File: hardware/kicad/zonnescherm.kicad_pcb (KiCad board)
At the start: 2 copper layers, 75 x 75 mm, 28 parts, among them K1 K1-ON/OFF, K2 K1-UP/DOWN, K3 K2-ON/OFF, K4 K2-UP/DOWN, P1 ARDUINO-ISP, P2 CONN_MAINS, P3 CONN_SUNSHADE1, P4 CONN_SUNSHADE2, P5 SWITCHES, U1 IRM-05-5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

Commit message: Added high voltage logo
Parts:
- added C6: 100n, Capacitors_SMD:C_0805_HandSoldering, B.Cu at (120.7, 109.2)
- added C7: 100n, Capacitors_SMD:C_0805_HandSoldering, B.Cu at (138.7, 109.2)
- added G***: LOGO, modex:high_voltage_logo, B.Cu at (158.5, 95.0)
- added R8: 390, Resistors_SMD:R_0805_HandSoldering, B.Cu at (117.9, 109.2)
- P5: footprint Pin_Headers:Pin_Header_Straight_2x04 -> Pin_Headers:Pin_Header_Straight_2x05
- moved G*** 0.36 mm to (132.6, 129.0)
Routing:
- net P3V3: track 77.0 -> 103.8 mm
- net GND: track 168.7 -> 161.4 mm
- net Net-(P5-Pad10): track 0.00 -> 3.21 mm
- net P5V: track 88.9 -> 91.7 mm

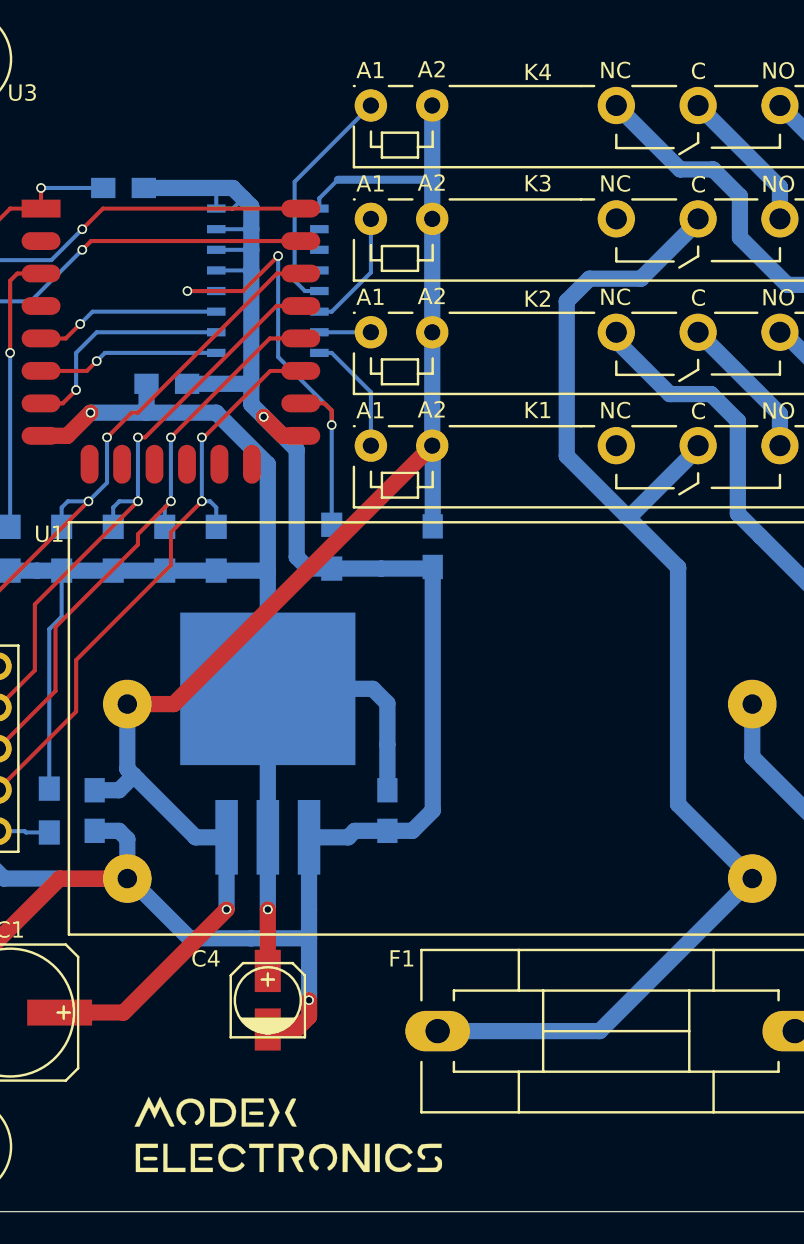
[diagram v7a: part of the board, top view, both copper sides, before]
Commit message: Added ESD logo and generated gerberfiles and drill files. Send design tot PCBWAY.com
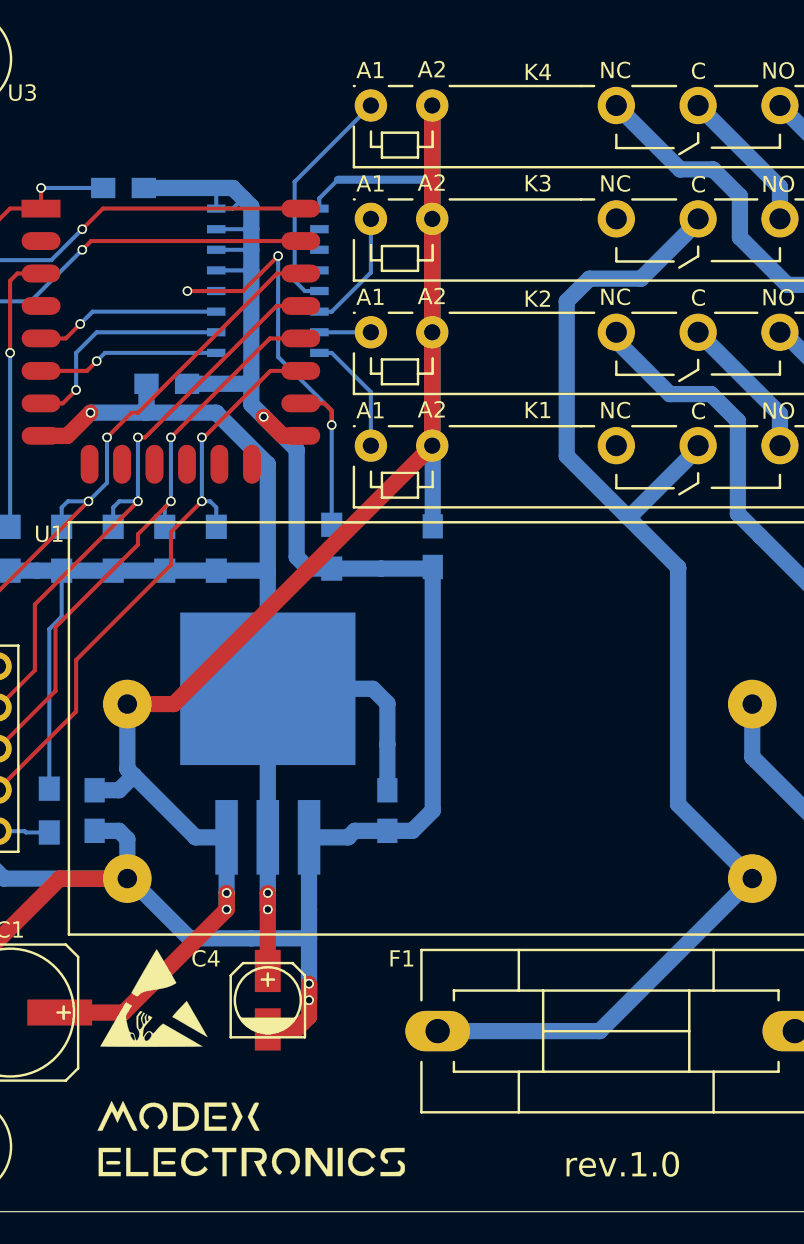
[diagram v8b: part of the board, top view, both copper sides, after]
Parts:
- added ?: , modex:esd, F.Cu at (124.5, 120.9)
- ? (x2): renamed from G***; value LOGO -> (none)
- moved ? 2.30 mm to (130.3, 129.3)
- renumbered REF** to ?
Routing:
- net P5V: track 91.7 -> 113.6 mm, vias 1 -> 2
- net GND: track 161.4 -> 162.4 mm, vias 2 -> 3
- net P3V3: track 103.8 -> 104.8 mm, vias 2 -> 3
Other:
- board text added: "rev.1.0"
